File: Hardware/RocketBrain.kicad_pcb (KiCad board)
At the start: 4 copper layers, 53.5 x 24 mm, 59 parts, among them J1 Screw_Terminal_01x02, J2 1x3 picoblade, J3 1x3 picoblade, J4 1x2 picoblade, J5 DM3CS-SF, J6 Screw_Terminal_01x02, J7 Screw_Terminal_01x02, Q1 G1003A, Q2 G1003A, U1 Pico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

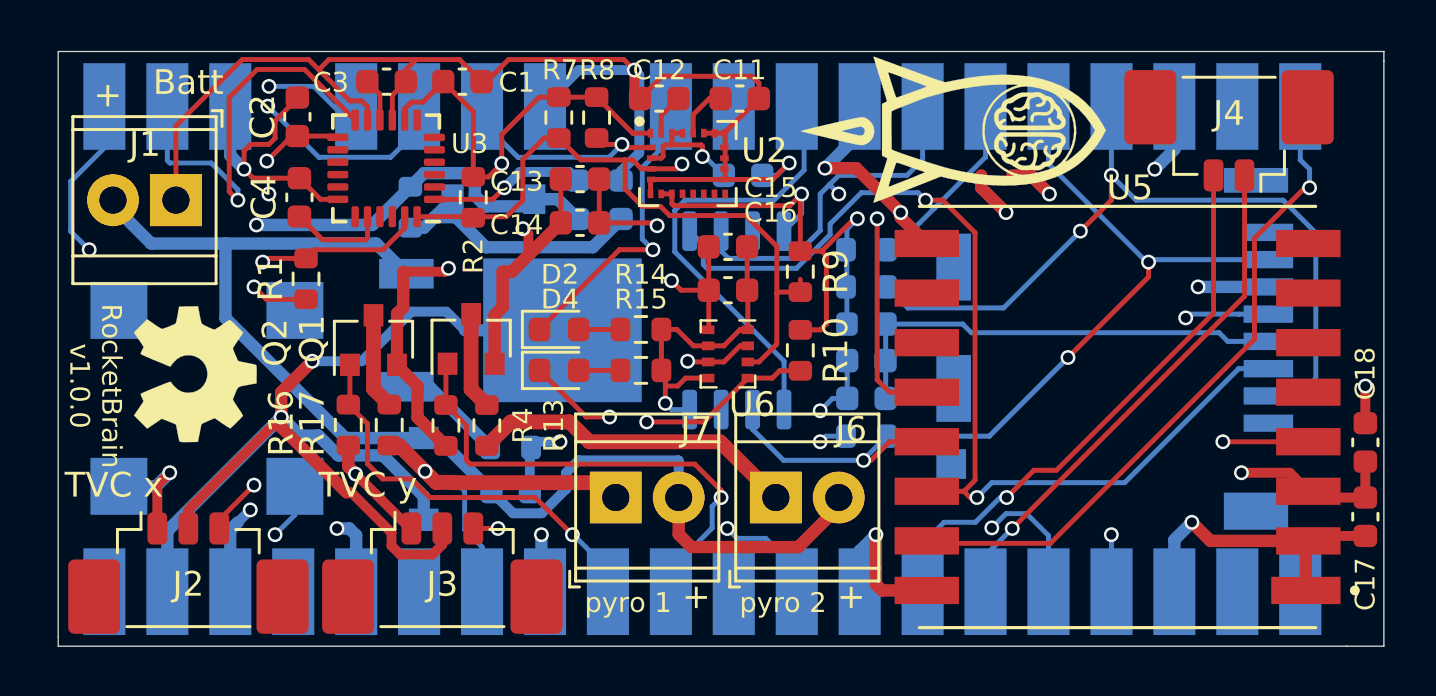
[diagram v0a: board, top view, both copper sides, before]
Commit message: Change regulator diode footprint, update routing
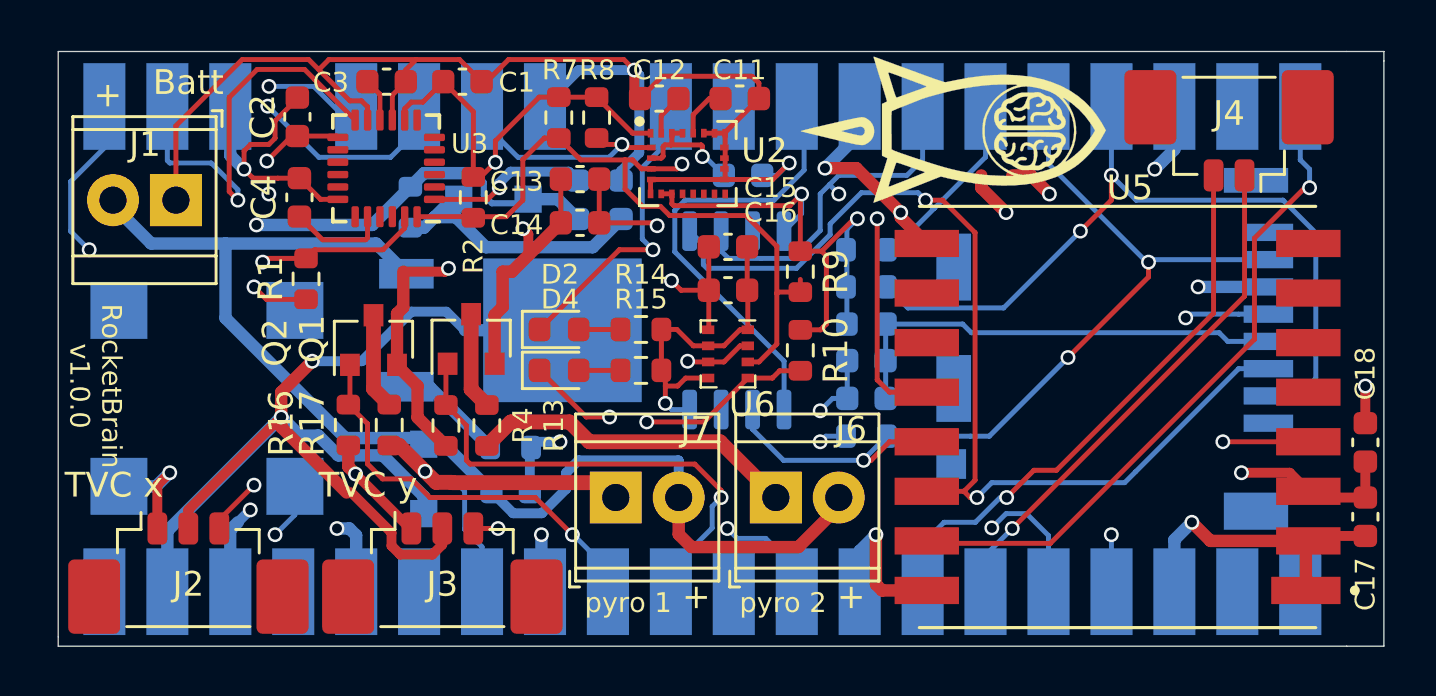
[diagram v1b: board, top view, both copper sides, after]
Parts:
- removed the G*** at (118.2, 77.0)
- D1, D3: footprint Diode_SMD:D_SOD-123 -> Diode_SMD:D_SOD-123F
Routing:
- net +5V: track 99.6 -> 99.1 mm
